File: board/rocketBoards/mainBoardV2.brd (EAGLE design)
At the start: 43 x 15 mm, 60 parts, among them J1 47346-0001

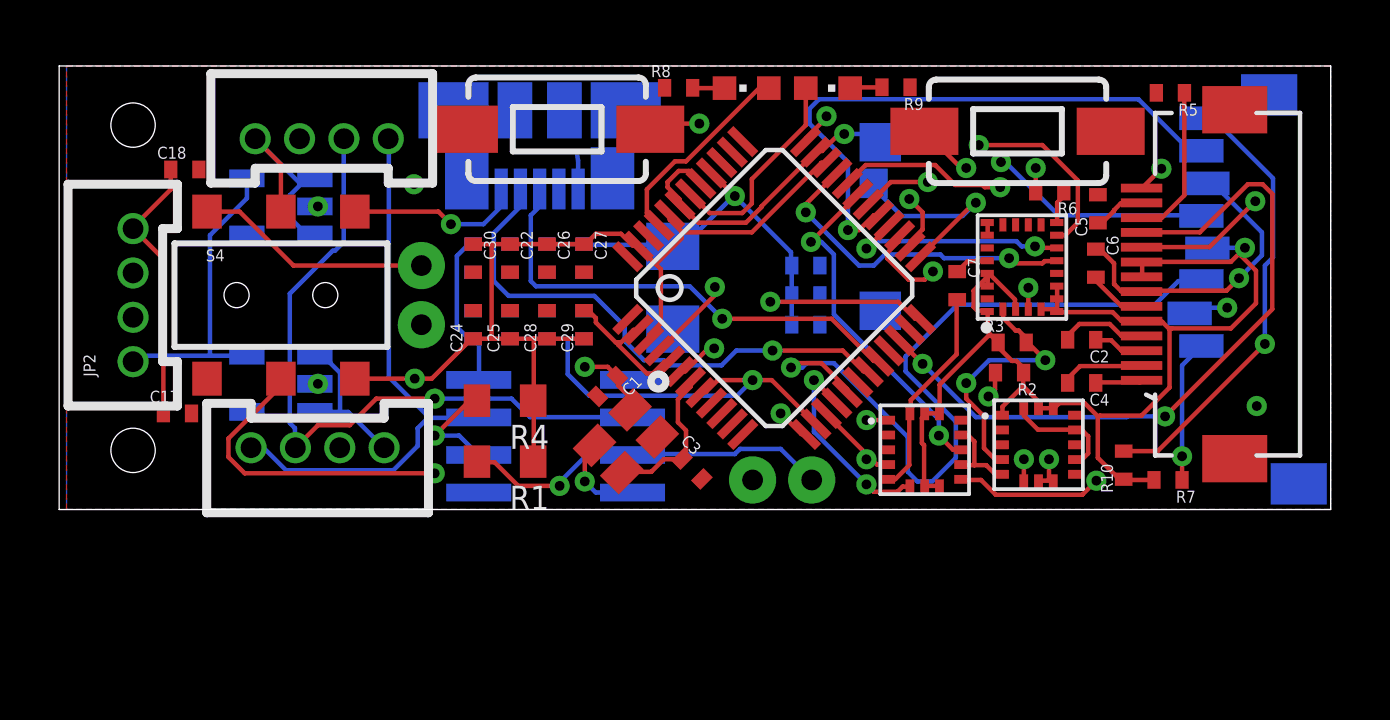
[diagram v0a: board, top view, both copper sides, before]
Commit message: added ThinMan basic board
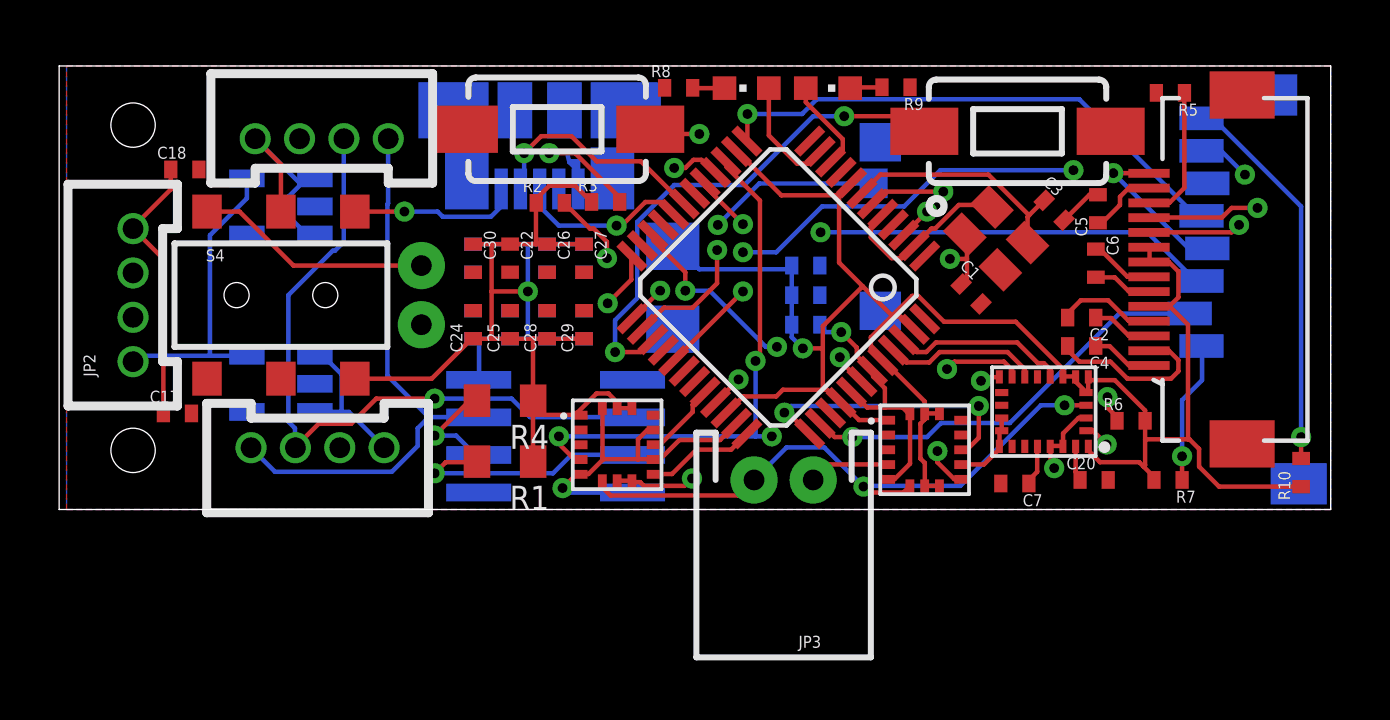
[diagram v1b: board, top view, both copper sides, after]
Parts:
- removed JP1: M02JST-PTH-2, SparkFun-Connectors:JST-2-PTH
- added JP3: M02JST-PTH-2, SparkFun-Connectors:JST-2-PTH
- moved C20 21.1 mm to (30.0, 1.00), flipped to the top, turned to 0 degrees
- moved R2 16.6 mm to (11.6, 10.4), turned to 0 degrees
- moved C3 15.1 mm to (28.6, 10.1)
- moved R3 14.5 mm to (13.5, 10.4)
- moved HIGHG_ACCEL 14.3 mm to (12.4, 0.69)
- moved C1 12.7 mm to (25.8, 7.29), turned to 315 degrees
- moved U$5 11.7 mm to (24.9, 9.38), turned to 315 degrees
- moved R6 8.22 mm to (31.2, 3.00), turned to 0 degrees
- moved C7 6.97 mm to (27.3, 0.88), turned to 180 degrees
- moved R10 6.01 mm to (37.0, 1.25)
- moved 9-AXIS 1.92 mm to (30.1, 4.81), turned to 180 degrees
- moved C4 1.25 mm to (29.6, 5.53)
- moved C2 0.75 mm to (29.6, 6.49)
- moved U$1 0.56 mm to (29.0, 8.12)
- moved U1 0.14 mm to (19.3, 7.51), turned to 135 degrees
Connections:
- net BARO_INT1: now also U1.37; no longer U1.31
- net BARO_INT2: now also U1.33; no longer U1.32
- net HIGHG_INT1: now also U1.32; no longer U1.37
- net HIGHG_INT2: now also U1.36; no longer U1.38
- net I2C0_SCL: now also JP3.1
- net I2C0_SDA: now also JP3.2
- net I2C1_SCL: no longer JP1.1
- net I2C1_SDA: no longer JP1.2
- net INT1_A/G: now also U1.45; no longer U1.28
- net INT2_A/G: now also U1.42; no longer U1.30
- net INT_M: no longer U1.33
- net LED_PIN: now also U1.10; no longer U1.42
- net LED_PIN2: now also U1.11; no longer U1.45
- net SSP1_SSEL: now also U1.38; no longer U1.36
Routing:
- net I2C0_SCL: track 16.0 -> 47.7 mm, vias 3 -> 5
- net PIO0_1: track 25.6 -> 0.00 mm, vias 2 -> 0
- net I2C0_SDA: track 22.1 -> 43.2 mm, vias 5 -> 4
- net I2C1_SCL: track 60.6 -> 47.8 mm
- net BARO_INT2: track 22.0 -> 10.5 mm
- net GND: track 47.3 -> 36.0 mm, vias 7 -> 2
- net INT_M: track 11.3 -> 0.00 mm, vias 2 -> 0
- net N$17: track 18.1 -> 7.86 mm
- net N$15: track 16.1 -> 5.90 mm
- net N$18: track 8.80 -> 17.6 mm
- net SSP1_MOSI: track 26.0 -> 18.2 mm, vias 1 -> 2
- net I2C1_SDA: track 43.6 -> 50.1 mm, vias 3 -> 4
- net N$1: track 1.14 -> 7.31 mm, vias 0 -> 2
- net DRDY_M: track 0.00 -> 5.90 mm
- net SSP1_SSEL: track 19.9 -> 14.4 mm, vias 2 -> 1
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- added copper zone on layer 2, net GND
